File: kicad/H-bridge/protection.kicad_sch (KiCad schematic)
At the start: 30 parts, among them U4 LT1011, U5 LM340MPX-5.0/NOPB, U6 74LVC1G373, U8 74AC14DR

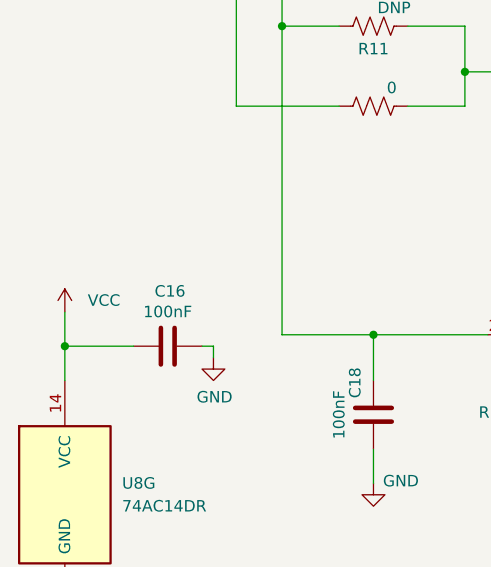
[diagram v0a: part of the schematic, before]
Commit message: Final Board schematics and layouts, Also added custom footprints that were made for the relay and terminal connector block.
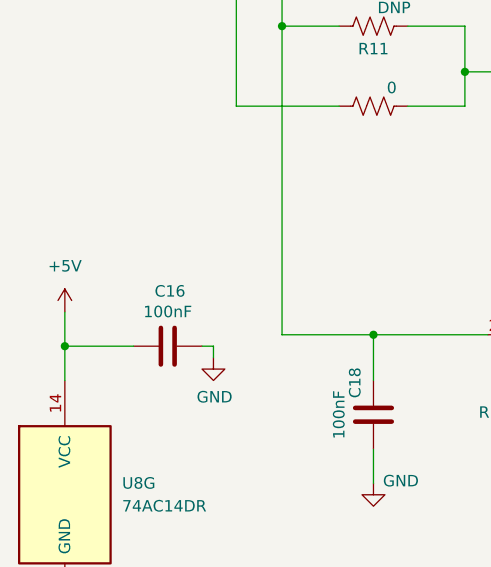
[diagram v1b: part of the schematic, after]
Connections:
- net +5V: now also C16.2, U8.14 (VCC)
- net VCC: no longer C16.2, U8.14 (VCC)
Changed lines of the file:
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@@
 (kicad_sch
-	(version 20231120)
+	(version 20250114)
 	(generator "eeschema")
-	(generator_version "8.0")
+	(generator_version "9.0")
 	(paper "A4")
+	(text "Change the threshold voltage range."
+		(exclude_from_sim no)
+		(at 106.172 152.654 0)
+		(effects
+			(font
+				(size 1.27 1.27)
+			)
+		)
+	)
 	(junction
 		(at 46.99 100.33)
@@
 		)
 	)
-	(text "Change the threshold voltage range."
-		(exclude_from_sim no)
-		(at 106.172 152.654 0)
-		(effects
-			(font
-				(size 1.27 1.27)
-			)
-		)
-	)
 	(hierarchical_label "output -"
 		(shape bidirectional)
 		(at 196.85 87.63 0)
-		(fields_autoplaced yes)
 		(effects
 			(font
@@
 		(shape input)
 		(at 40.64 76.2 180)
-		(fields_autoplaced yes)
 		(effects
 			(font
@@
 		(shape input)
 		(at 44.45 100.33 180)
-		(fields_autoplaced yes)
 		(effects
 			(font
@@
 		(shape bidirectional)
 		(at 196.85 76.2 0)
-		(fields_autoplaced yes)
 		(effects
 			(font
@@
 	)
 	(symbol
+		(lib_id "power:+5V")
+		(at 27.94 149.86 0)
+		(unit 1)
+		(exclude_from_sim no)
+		(in_bom yes)
+		(on_board yes)
+		(dnp no)
+		(fields_autoplaced yes)
+		(property "Reference" "#PWR023"
+			(at 27.94 153.67 0)
+			(effects
+				(font
+					(size 1.27 1.27)
+				)
+				(hide yes)
+			)
+		)
+		(property "Value" "+5V"
+			(at 27.94 144.78 0)
+			(effects
+				(font
+					(size 1.27 1.27)
+				)
+			)
+		)
+		(property "Footprint" ""
+			(at 27.94 149.86 0)
+			(effects
+				(font
+					(size 1.27 1.27)
+				)
+				(hide yes)
+			)
+		)
+		(property "Datasheet" ""
+			(at 27.94 149.86 0)
+			(effects
+				(font
+					(size 1.27 1.27)
+				)
+				(hide yes)
+			)
+		)
+		(property "Description" "Power symbol creates a global label with name \"+5V\""
+			(at 27.94 149.86 0)
+			(effects
+				(font
+					(size 1.27 1.27)
+				)
+				(hide yes)
+			)
+		)
+		(pin "1"
+		)
+		(instances
+			(project "H_bridge"
+				(path "/8510e844-3def-44d1-bcab-3572b2a43923/f24dd8f5-dede-4199-a3bf-173aa3d1c3ca"
+					(reference "#PWR023")
+					(unit 1)
+				)
+			)
+		)
+	)
+	(symbol
 		(lib_id "Coil_speedifier-rescue:GND-power")
 		(at 44.45 154.94 0)
@@
 					(unit 1)
 				)
-			)
-		)
-	)
-	(symbol
-		(lib_id "power:VCC")
-		(at 27.94 149.86 0)
-		(unit 1)
-		(exclude_from_sim no)
-		(in_bom yes)
-		(on_board yes)
-		(dnp no)
-		(fields_autoplaced yes)
-		(property "Reference" "#PWR023"
-			(at 27.94 153.67 0)
-			(effects
-				(font
-					(size 1.27 1.27)
-				)
-				(hide yes)
-			)
-		)
-		(property "Value" "VCC"
-			(at 30.48 148.5899 0)
-			(effects
-				(font
-					(size 1.27 1.27)
-				)
-				(justify left)
-			)
-		)
-		(property "Footprint" ""
-			(at 27.94 149.86 0)
-			(effects
-				(font
-					(size 1.27 1.27)
-				)
-				(hide yes)
-			)
-		)
-		(property "Datasheet" ""
-			(at 27.94 149.86 0)
-			(effects
-				(font
-					(size 1.27 1.27)
-				)
-				(hide yes)
-			)
-		)
-		(property "Description" "Power symbol creates a global label with name \"VCC\""
-			(at 27.94 149.86 0)
-			(effects
-				(font
-					(size 1.27 1.27)
-				)
-				(hide yes)
-			)
-		)
-		(pin "1"
-		)
-		(instances
-			(project "H_bridge"
-				(path "/8510e844-3def-44d1-bcab-3572b2a43923/f24dd8f5-dede-4199-a3bf-173aa3d1c3ca"
-					(reference "#PWR023")
-					(unit 1)
-				)
